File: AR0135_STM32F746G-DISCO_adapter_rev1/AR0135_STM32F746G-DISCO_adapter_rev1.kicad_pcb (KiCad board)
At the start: 2 copper layers, 40 x 40 mm, 7 parts, among them J1 Conn_01x30, J2 Conn_01x30, J3 Conn_01x04

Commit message: Gerber files generated
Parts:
- added J4: Conn_01x10, Connector_PinHeader_2.54mm:PinHeader_1x10_P2.54mm_Vertical, F.Cu at (45.0, 41.5)
- J1: footprint Connector_FFC-FPC:Hirose_FH12-30S-0.5SH_1x30-1MP_P0.50mm_Horizontal -> sense_fp:ArduCam_FPC_30pin_P0.50mm_Horizontal
- J3: value Conn_01x04 -> Conn_01x10; footprint Connector_PinHeader_2.54mm:PinHeader_1x04_P2.54mm_Vertical -> Connector_PinHeader_2.54mm:PinHeader_1x10_P2.54mm_Vertical
- moved J3 26.5 mm to (15.0, 18.5)
- moved J2 12.1 mm to (30.0, 45.0)
- moved J1 9.51 mm to (30.0, 15.0), turned to 180 degrees
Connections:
- J1 pad 15: /D3 -> (no net)
- J1 pad 16: /D2 -> (no net)
- J1 pad 17: /D1 -> (no net)
- J1 pad 18: /D0 -> (no net)
- J2 pad 12: Net-(J2-Pad12) -> (no net)
- J2 pad 13: Net-(J2-Pad13) -> (no net)
- J2 pad 18: Net-(J2-Pad18) -> (no net)
- J2 pad 2: Net-(J2-Pad2) -> (no net)
- J2 pad 22: Net-(J2-Pad22) -> (no net)
- J2 pad 24: Net-(J2-Pad24) -> (no net)
- J2 pad 3: Net-(J2-Pad3) -> (no net)
- J3 pad 3: /3V3 -> /DCMI_VSYNC
- J3 pad 4: /GND -> /DCMI_HSYNC
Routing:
- net /Camera_CLK: track 0.00 -> 78.5 mm, vias 0 -> 1
- net /DCMI_PIXCK: track 0.00 -> 62.3 mm, vias 0 -> 3
- net /3V3: track 0.00 -> 57.8 mm
- net /GND: track 0.00 -> 51.3 mm, vias 0 -> 2
- net /D4: track 0.00 -> 51.0 mm, vias 0 -> 2
- net /D5: track 0.00 -> 50.9 mm, vias 0 -> 2
- net /D6: track 0.00 -> 49.3 mm, vias 0 -> 2
- net /DCMI_VSYNC: track 0.00 -> 48.0 mm, vias 0 -> 1
- net /DCMI_HSYNC: track 0.00 -> 46.7 mm, vias 0 -> 1
- net /D7: track 0.00 -> 45.8 mm, vias 0 -> 2
- net /DCMI_PWR_EN: track 0.00 -> 42.0 mm, vias 0 -> 1
- net /D8: track 0.00 -> 41.7 mm, vias 0 -> 2
- net /DCMI_NRST: track 0.00 -> 40.7 mm
- net /D9: track 0.00 -> 40.5 mm, vias 0 -> 2
- net /D11: track 0.00 -> 40.5 mm, vias 0 -> 2
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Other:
- board text added: "3V3"
- board text added: "Camera_CLK"
- board text added: "D10"
- board text added: "D11"
- board text added: "D4"
- board text added: "D5"
- board text added: "D6"
- board text added: "D7"
- board text added: "D8"
- board text added: "D9"
- board text added: "FLASH"
- board text added: "GND"
- board text added: "HSYNC"
- board text added: "NRST"
- board text added: "PIXCK"
- board text added: "PWR_EN"
- board text added: "SCL"
- board text added: "SDA"
- board text added: "TRIGGER"
- board text added: "VSYNC"

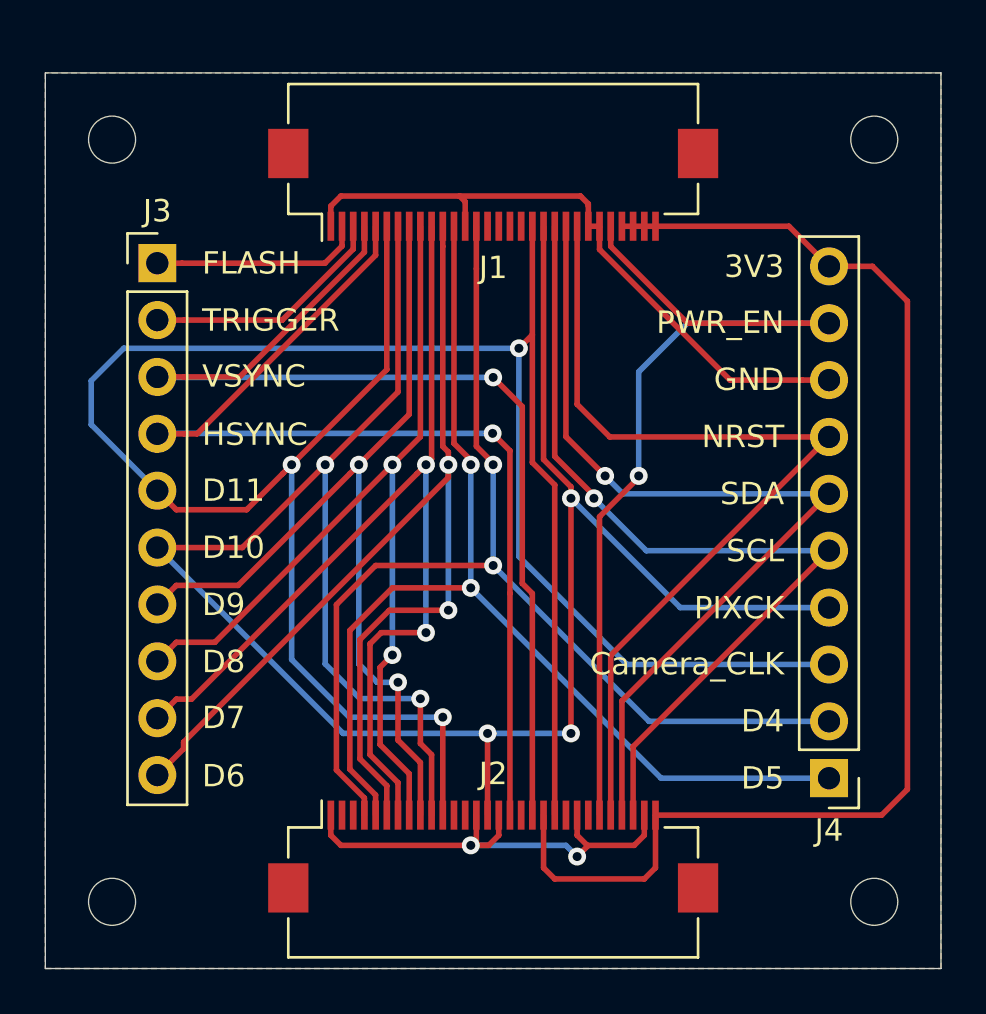
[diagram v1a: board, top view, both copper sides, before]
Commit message: updated J2 footprint
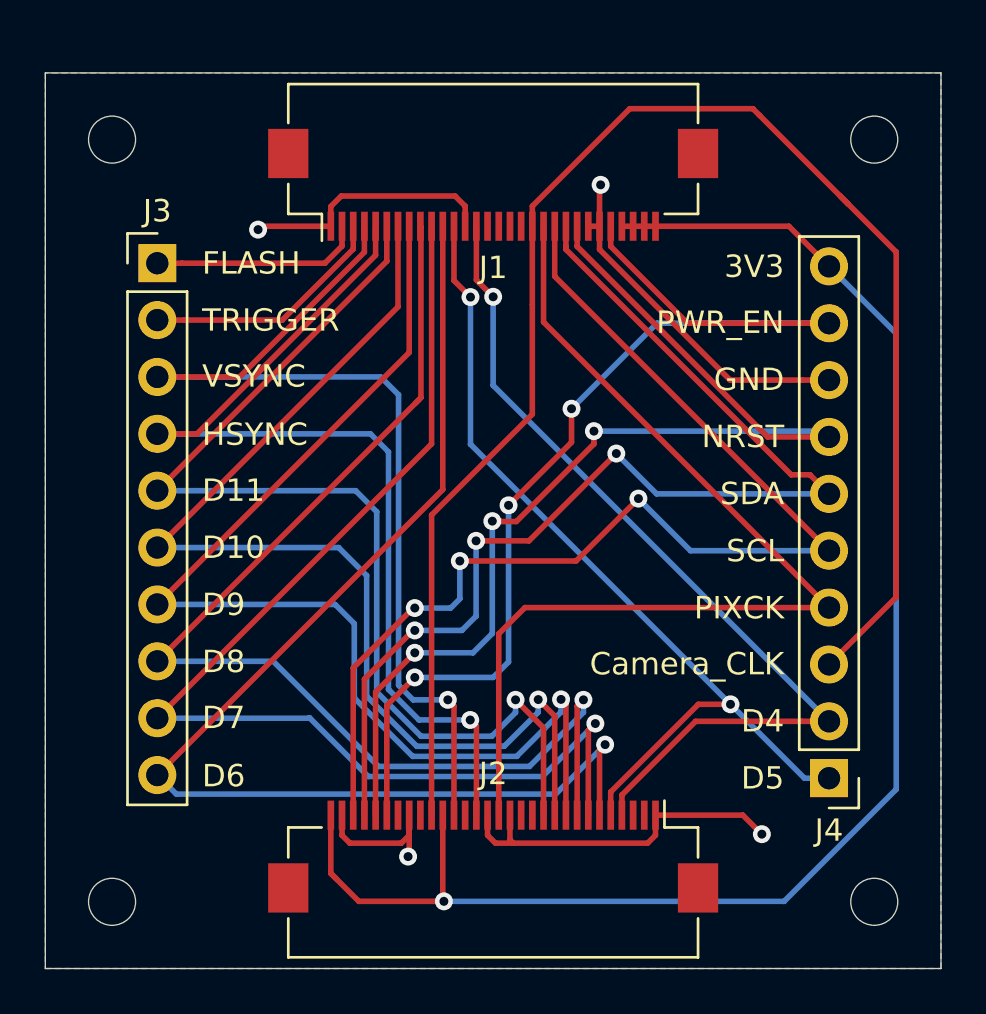
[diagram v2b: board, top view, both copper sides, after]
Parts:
- J2: footprint Connector_FFC-FPC:Hirose_FH12-30S-0.5SH_1x30-1MP_P0.50mm_Horizontal -> sense:ArduCam_FPC_30pin_P0.50mm_Horizontal
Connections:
- J1 pad 15: (no net) -> /D3
- J1 pad 16: (no net) -> /D2
- J1 pad 17: (no net) -> /D1
- J1 pad 18: (no net) -> /D0
- J2 pad 12: (no net) -> Net-(J2-Pad12)
- J2 pad 13: (no net) -> Net-(J2-Pad13)
- J2 pad 18: (no net) -> Net-(J2-Pad18)
- J2 pad 2: (no net) -> Net-(J2-Pad2)
- J2 pad 22: (no net) -> Net-(J2-Pad22)
- J2 pad 24: (no net) -> Net-(J2-Pad24)
- J2 pad 3: (no net) -> Net-(J2-Pad3)
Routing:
- net /DCMI_PIXCK: track 62.3 -> 45.6 mm, vias 3 -> 0
- net /DCMI_SCL: track 39.8 -> 52.5 mm, vias 1 -> 3
- net /3V3: track 57.8 -> 69.3 mm, vias 0 -> 1
- net /D4: track 51.0 -> 40.1 mm, vias 2 -> 1
- net /D5: track 50.9 -> 40.2 mm
- net /DCMI_SDA: track 40.4 -> 51.0 mm, vias 1 -> 3
- net /D8: track 41.7 -> 52.3 mm, vias 2 -> 1
- net /D9: track 40.5 -> 51.0 mm, vias 2 -> 1
- net /D10: track 40.2 -> 49.3 mm, vias 2 -> 1
- net /DCMI_NRST: track 40.7 -> 49.6 mm, vias 0 -> 3
- net /Camera_CLK: track 78.5 -> 69.9 mm, vias 1 -> 0
- net /D11: track 40.5 -> 48.0 mm, vias 2 -> 1
- net /D7: track 45.8 -> 52.9 mm, vias 2 -> 1
- net /DCMI_PWR_EN: track 42.0 -> 48.8 mm, vias 1 -> 3
- net /D6: track 49.3 -> 54.3 mm, vias 2 -> 1
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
